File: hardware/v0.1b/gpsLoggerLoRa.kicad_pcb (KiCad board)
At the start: 4 copper layers, 40.9 x 72.7 mm, 121 parts, among them J1 USB_C_Receptacle, J2 JST GH, J3 DF12 - 10P, J4 CTX TAG Connect, Q1 FG6943010R, SW1 SW_Push, U1 SKY13373, U2 MCP73832, U3 NCP167, U4 SKY13373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

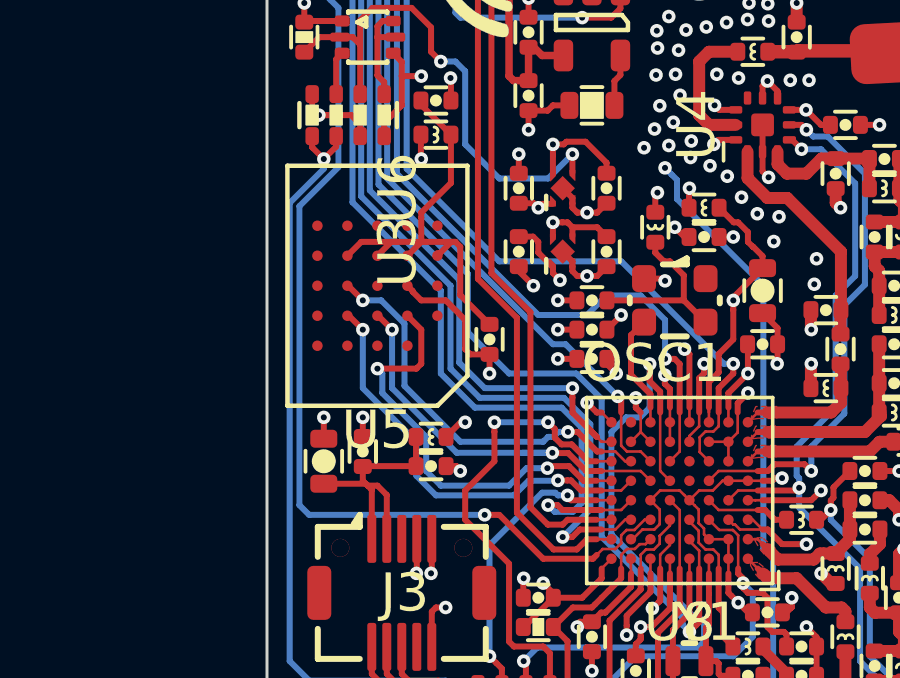
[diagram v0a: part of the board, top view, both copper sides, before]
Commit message: Fix to FLASH footprint.
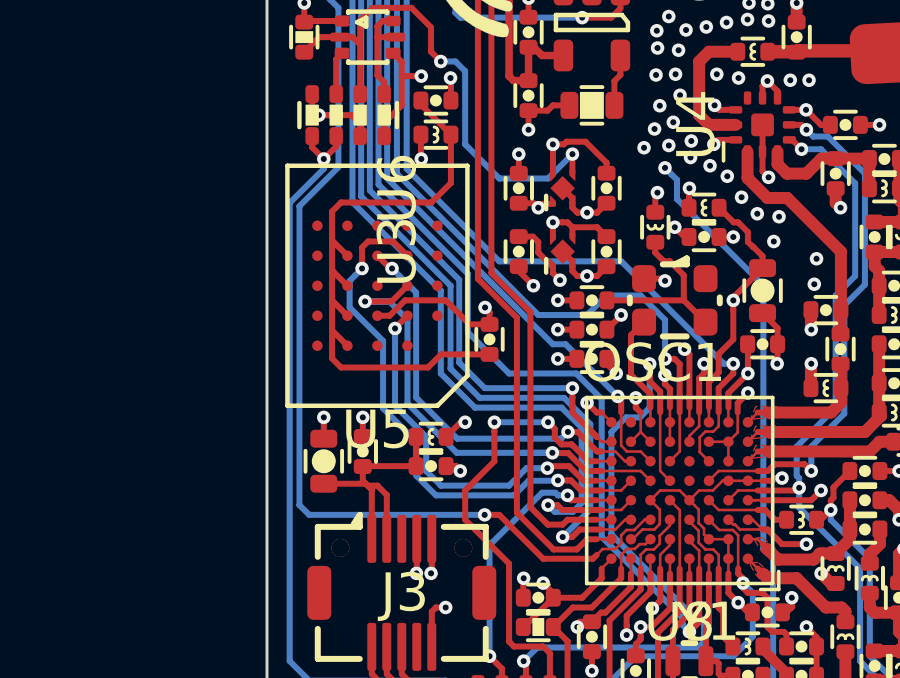
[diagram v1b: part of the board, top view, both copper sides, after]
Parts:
- turned C44 to 90 degrees
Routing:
- net Net-(C43-Pad1): track 15.1 -> 21.0 mm
- net /memio/DQ1: track 14.2 -> 18.4 mm
- net /SAMR34/FLASH_CS#: track 13.5 -> 16.3 mm
- net /SAMR34/FLASH_CLK: track 14.3 -> 12.6 mm
